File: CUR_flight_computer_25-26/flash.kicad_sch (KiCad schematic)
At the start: 21 parts, among them J6 Micro_SD_Card, U10 W25Q32JVSS

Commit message: Replace SS12 with BAT54
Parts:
- removed R21, R22, R23, R24, R25: 22, Resistor_SMD:R_0603_1608Metric, symbol Device:R_Small_US
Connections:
- net FLASH_CLK: now also U10.6 (CLK)
- net FLASH_IO0: now also U10.5 (DI/IO_{0})
- net FLASH_IO1: now also U10.2 (DO/IO_{1})
- net FLASH_IO2: now also R26.2, U10.3 (~{WP}/IO_{2})
- net FLASH_IO3: now also R27.2, U10.7 (~{HOLD}/~{RESET}/IO_{3})

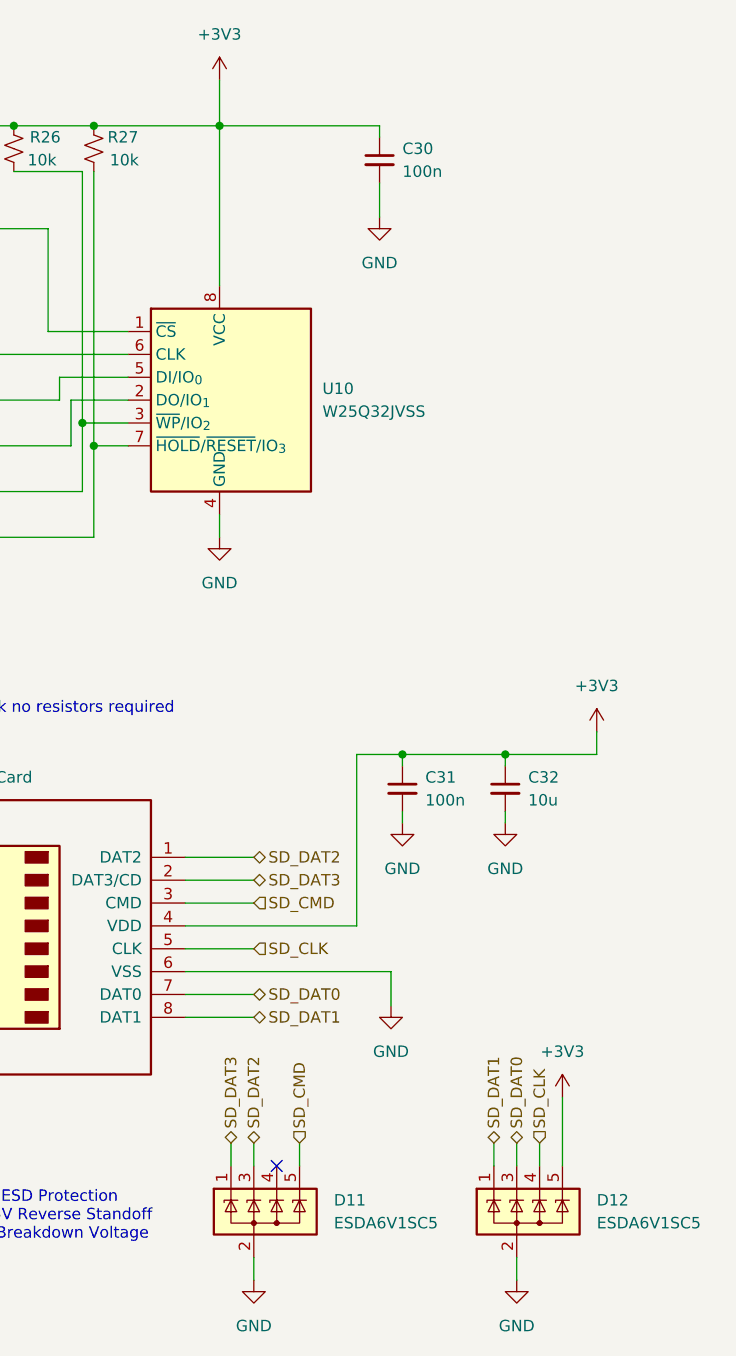
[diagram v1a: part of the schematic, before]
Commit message: Apply MPNs for capacitors and connectors
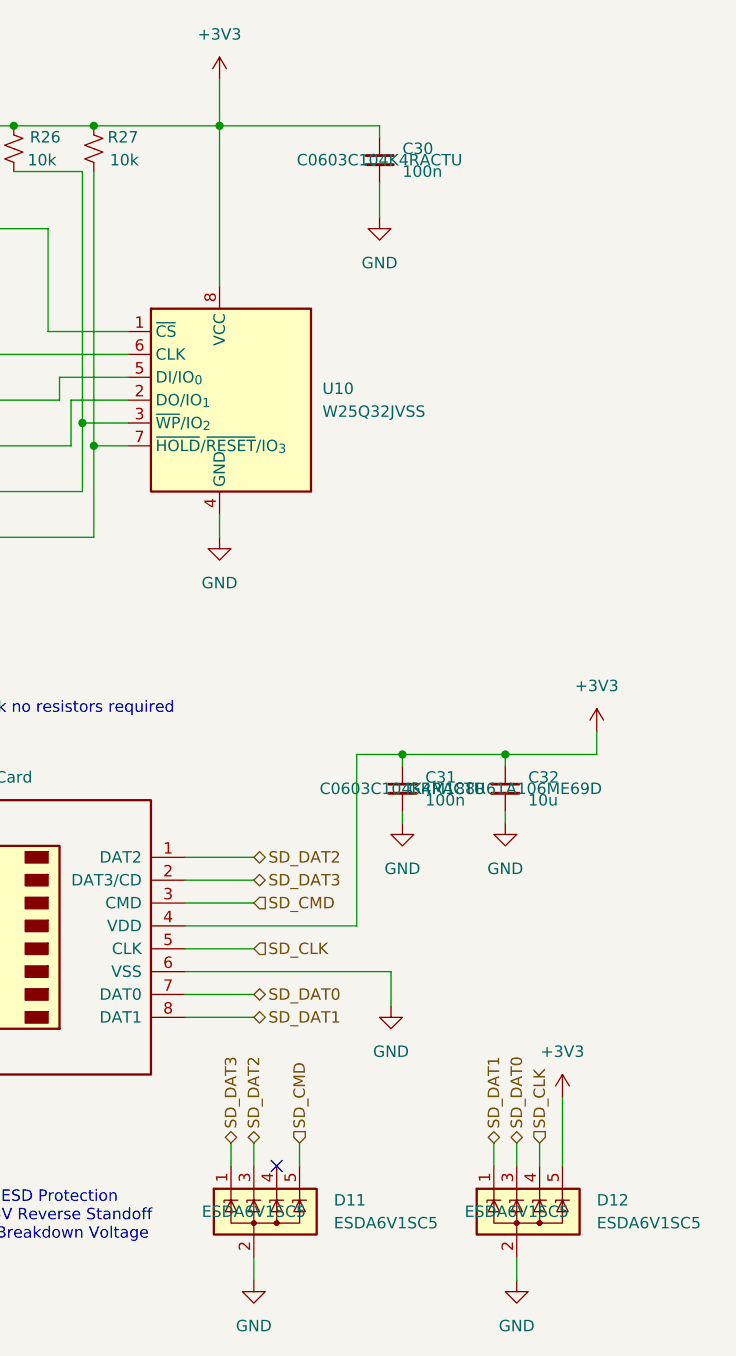
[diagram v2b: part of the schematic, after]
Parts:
- C30, C31: MPN (none) -> C0603C104K4RACTU
- C32: MPN (none) -> GRM188R61A106ME69D
- D11, D12: MPN (none) -> ESDA6V1SC5
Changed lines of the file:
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@@
+			)
+		)
+		(property "MPN" "ESDA6V1SC5"
+			(at 78.74 152.4 0)
+			(effects
+				(font
+					(size 1.27 1.27)
+				)
 			)
 		)
@@
 				)
 				(hide yes)
+			)
+		)
+		(property "MPN" "GRM188R61A106ME69D"
+			(at 106.68 105.41 0)
+			(effects
+				(font
+					(size 1.27 1.27)
+				)
 			)
 		)
@@
 			)
 		)
+		(property "MPN" "C0603C104K4RACTU"
+			(at 92.71 35.56 0)
+			(effects
+				(font
+					(size 1.27 1.27)
+				)
+			)
+		)
 		(pin "1"
 		)
@@
 			)
 		)
+		(property "MPN" "C0603C104K4RACTU"
+			(at 95.25 105.41 0)
+			(effects
+				(font
+					(size 1.27 1.27)
+				)
+			)
+		)
 		(pin "1"
 		)
@@
 			)
 		)
+		(property "MPN" "ESDA6V1SC5"
+			(at 107.95 152.4 0)
+			(effects
+				(font
+					(size 1.27 1.27)
+				)
+			)
+		)

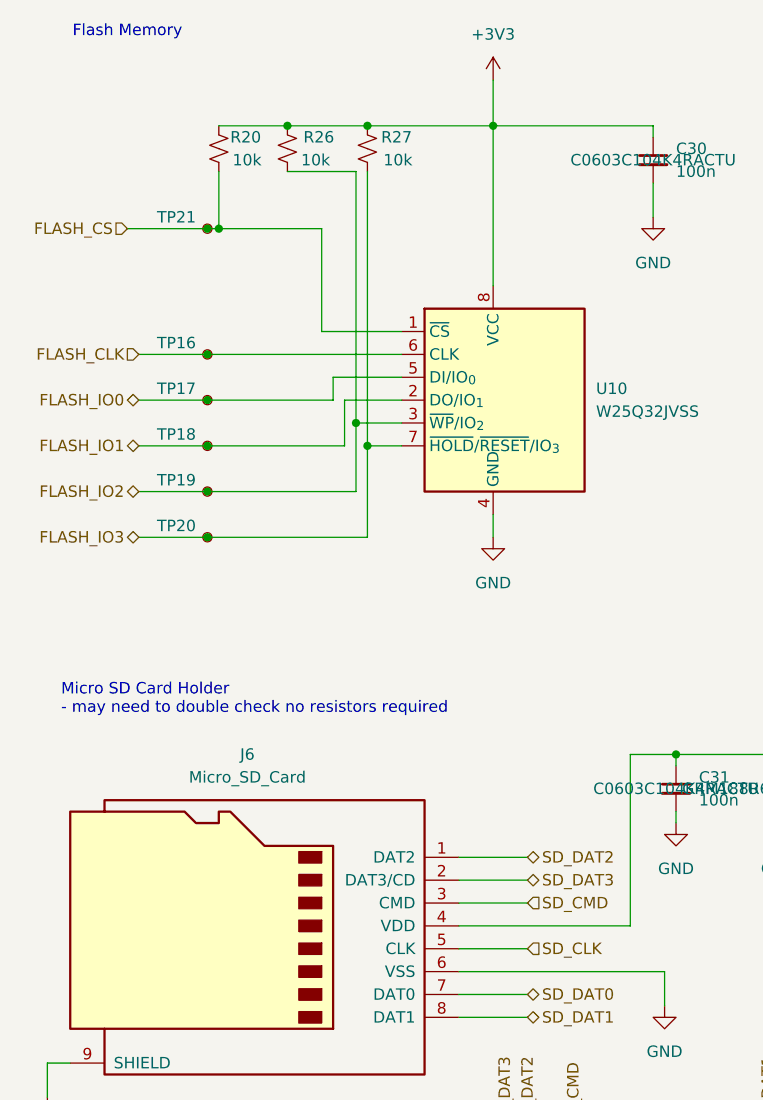
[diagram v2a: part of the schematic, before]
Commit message: Add MPNs for ICs
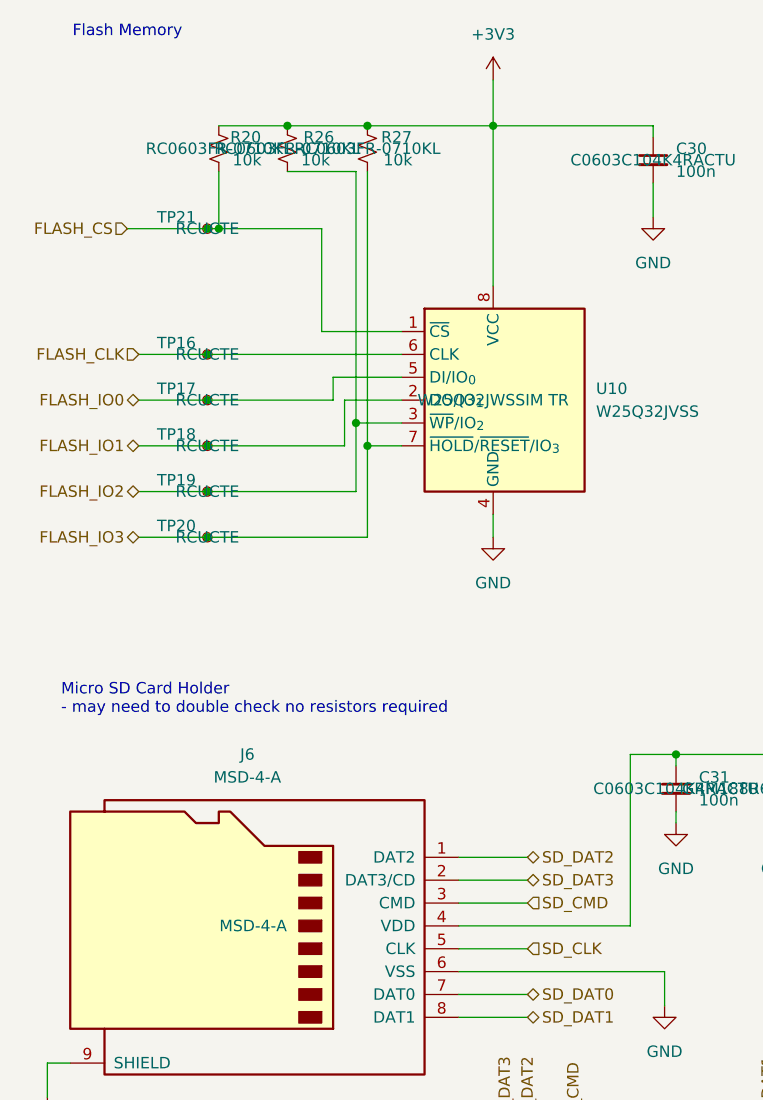
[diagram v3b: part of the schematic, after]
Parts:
- J6: value Micro_SD_Card -> MSD-4-A; MPN (none) -> MSD-4-A
- R20, R26, R27: MPN (none) -> RC0603FR-0710KL
- TP16, TP17, TP18, TP19, TP20, TP21: value TestPoint_Small -> RCUCTE; MPN (none) -> RCUCTE
- U10: MPN (none) -> W25Q32JWSSIM TR
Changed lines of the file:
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@@
+			)
+		)
+		(property "MPN" "RC0603FR-0710KL"
+			(at 44.45 34.29 0)
+			(effects
+				(font
+					(size 1.27 1.27)
+				)
 			)
 		)
@@
 			)
 		)
-		(property "Value" "TestPoint_Small"
+		(property "Value" "RCUCTE"
 			(at 41.91 78.7399 0)
 			(effects
@@
 				)
 				(hide yes)
+			)
+		)
+		(property "MPN" "RCUCTE"
+			(at 43.18 77.47 0)
+			(effects
+				(font
+					(size 1.27 1.27)
+				)
 			)
 		)
@@
 			)
 		)
-		(property "Value" "TestPoint_Small"
+		(property "Value" "RCUCTE"
 			(at 43.942 53.594 0)
 			(effects
@@
 				)
 				(hide yes)
+			)
+		)
+		(property "MPN" "RCUCTE"
+			(at 43.18 57.15 0)
+			(effects
+				(font
+					(size 1.27 1.27)
+				)
 			)
 		)
@@
 			)
 		)
-		(property "Value" "TestPoint_Small"
+		(property "Value" "RCUCTE"
 			(at 41.91 73.6599 0)
 			(effects
@@
 			)
 		)
+		(property "MPN" "RCUCTE"
+			(at 43.18 72.39 0)
+			(effects
+				(font
+					(size 1.27 1.27)
+				)
+			)
+		)
 		(pin "1"
 		)
@@
 				)
 				(hide yes)
+			)
+		)
+		(property "MPN" "RC0603FR-0710KL"
+			(at 60.96 34.29 0)
+			(effects
+				(font
+					(size 1.27 1.27)
+				)
 			)
 		)
@@
 			)
 		)
-		(property "Value" "TestPoint_Small"
+		(property "Value" "RCUCTE"
 			(at 41.91 44.4499 0)
 			(effects
@@
 				)
 				(hide yes)
+			)
+		)
+		(property "MPN" "RCUCTE"
+			(at 43.18 43.18 0)
+			(effects
+				(font
+					(size 1.27 1.27)
+				)
 			)
 		)
@@
 			)
 		)
-		(property "Value" "Micro_SD_Card"
+		(property "Value" "MSD-4-A"
 			(at 47.625 104.14 0)
 			(effects
@@
 				)
 				(hide yes)
+			)
+		)
+		(property "MPN" "MSD-4-A"
+			(at 48.26 120.65 0)
+			(effects
+				(font
+					(size 1.27 1.27)
+				)
 			)
 		)
@@
 			)
 		)
+		(property "MPN" "W25Q32JWSSIM TR"
+			(at 74.93 62.23 0)
+			(effects
+				(font
+					(size 1.27 1.27)
+				)
+			)
+		)
 		(pin "7"
 		)
@@
 			)
 		)
-		(property "Value" "TestPoint_Small"
+		(property "Value" "RCUCTE"
 			(at 41.91 63.4999 0)
 			(effects
@@
 				)
 				(hide yes)
+			)
+		)
+		(property "MPN" "RCUCTE"
+			(at 43.18 62.23 0)
+			(effects
+				(font
+					(size 1.27 1.27)
+				)
 			)
 		)
@@
 			)
 		)
-		(property "Value" "TestPoint_Small"
+		(property "Value" "RCUCTE"
 			(at 41.91 68.5799 0)
 			(effects
@@
 			)
 		)
+		(property "MPN" "RCUCTE"
+			(at 43.18 67.31 0)
+			(effects
+				(font
+					(size 1.27 1.27)
+				)
+			)
+		)
 		(pin "1"
 		)
@@
 			)
 		)
+		(property "MPN" "RC0603FR-0710KL"
+			(at 52.07 34.29 0)
+			(effects
+				(font
+					(size 1.27 1.27)
+				)
+			)
+		)

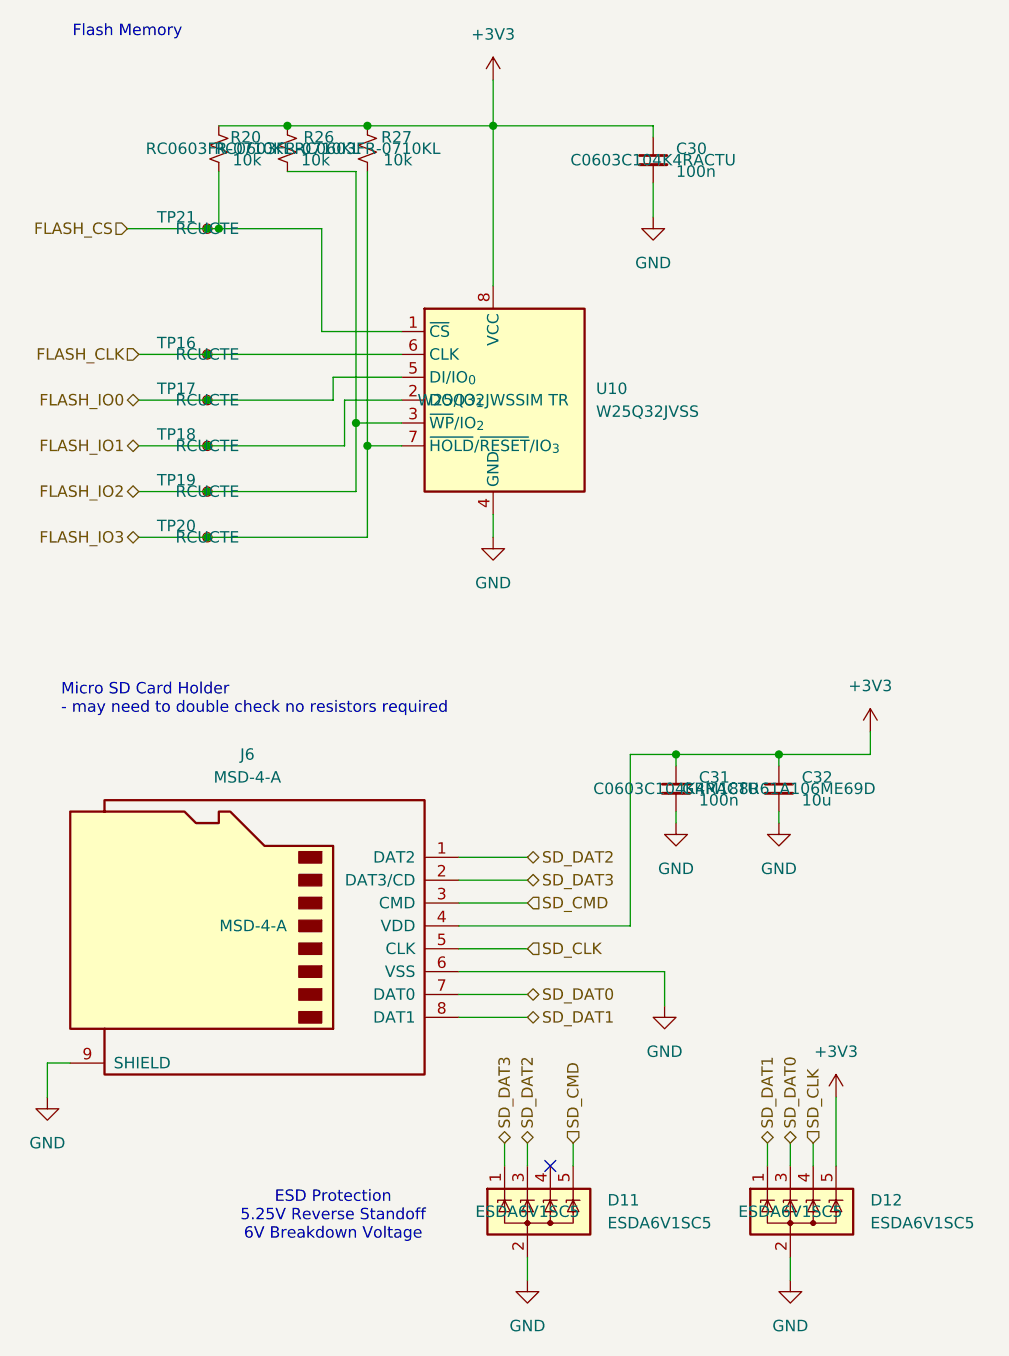
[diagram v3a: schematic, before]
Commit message: Hide MPNs
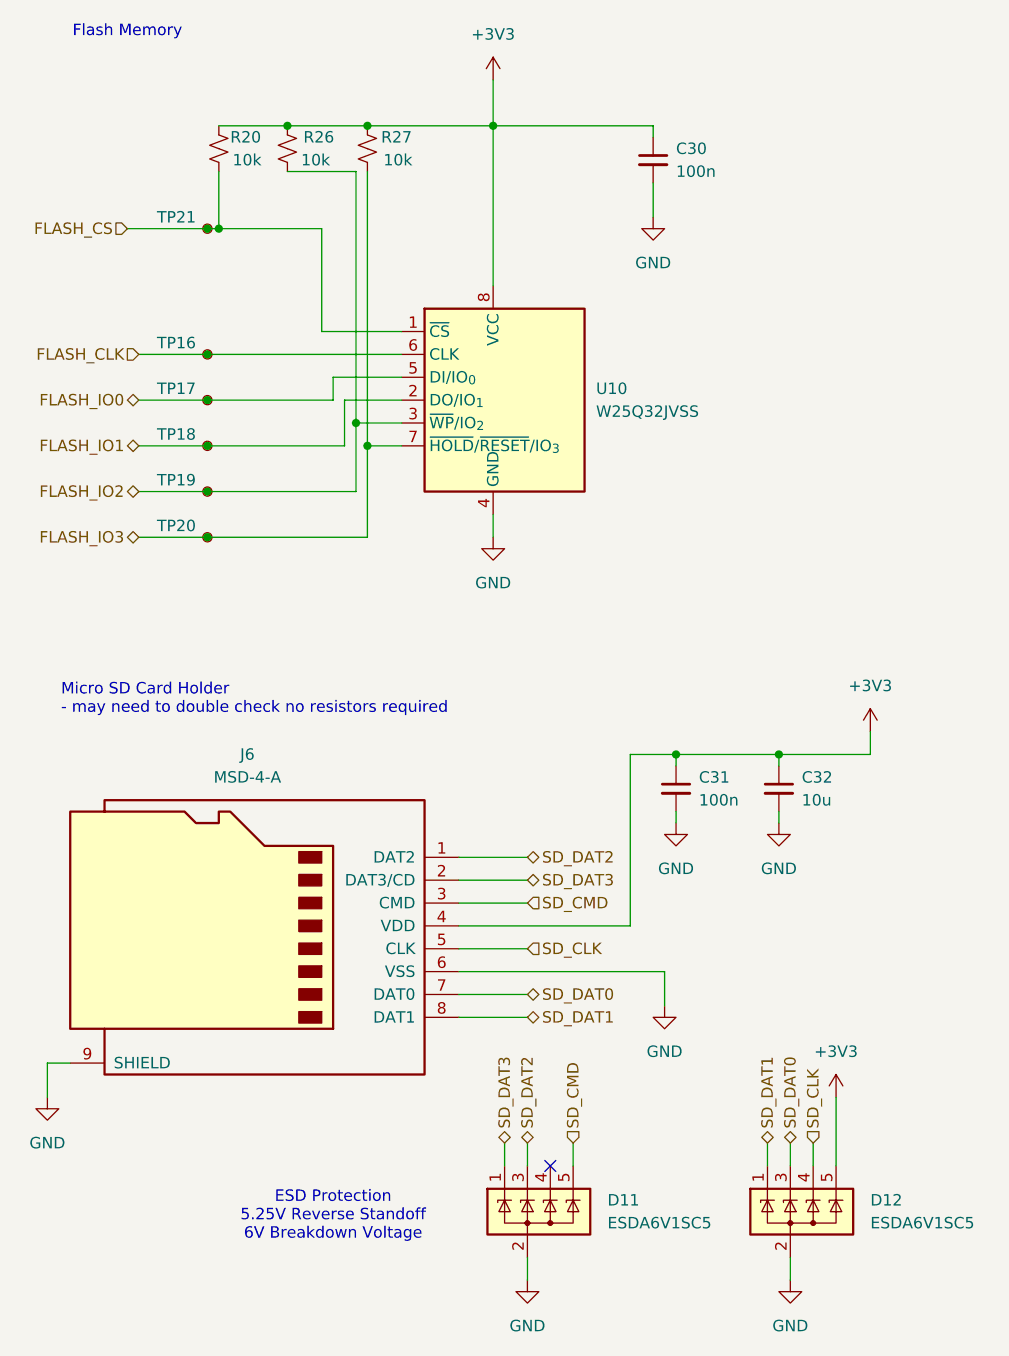
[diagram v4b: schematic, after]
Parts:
- U10: MPN W25Q32JWSSIM TR -> BY25Q128ESSIG(T)
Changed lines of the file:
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@@
 					(size 1.27 1.27)
 				)
+				(hide yes)
 			)
 		)
@@
 					(size 1.27 1.27)
 				)
+				(hide yes)
 			)
 		)
@@
 					(size 1.27 1.27)
 				)
+				(hide yes)
 			)
 		)
@@
 					(size 1.27 1.27)
 				)
+				(hide yes)
 			)
 		)
@@
 					(size 1.27 1.27)
 				)
+				(hide yes)
 			)
 		)
@@
 					(size 1.27 1.27)
 				)
+				(hide yes)
 			)
 		)
@@
 					(size 1.27 1.27)
 				)
+				(hide yes)
 			)
 		)
@@
 					(size 1.27 1.27)
 				)
+				(hide yes)
 			)
 		)
@@
 					(size 1.27 1.27)
 				)
+				(hide yes)
 			)
 		)
@@
 					(size 1.27 1.27)
 				)
+				(hide yes)
 			)
 		)
@@
 					(size 1.27 1.27)
 				)
+				(hide yes)
 			)
 		)
@@
 					(size 1.27 1.27)
 				)
+				(hide yes)
 			)
 		)
@@
 			)
 		)
-		(property "MPN" "W25Q32JWSSIM TR"
+		(property "MPN" "BY25Q128ESSIG(T)"
 			(at 74.93 62.23 0)
 			(effects
@@
 					(size 1.27 1.27)
 				)
+				(hide yes)
 			)
 		)
@@
 					(size 1.27 1.27)
 				)
+				(hide yes)
 			)
 		)
@@
 					(size 1.27 1.27)
 				)
+				(hide yes)
 			)
 		)
@@
 					(size 1.27 1.27)
 				)
-			)
-		)
+				(hide yes)
+			)
+		)
